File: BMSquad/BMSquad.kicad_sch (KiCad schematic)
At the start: 35 parts, among them J1 USB_C_Receptacle_USB2.0_16P, J2 OUT_1 +, J3 BAT_1 +, J4 OUT_1 -, J5 BAT_1 -, J6 OUT_2 +, J7 OUT_2 -, J8 BAT_2 +, J9 BAT_2 -, U1 TP4056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

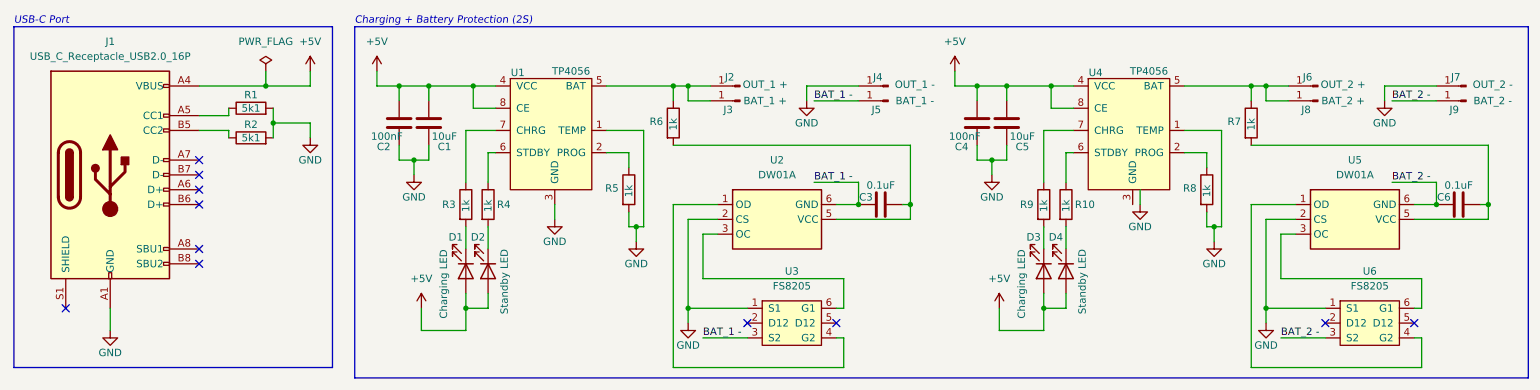
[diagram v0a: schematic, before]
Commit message: added hierarchical sheets
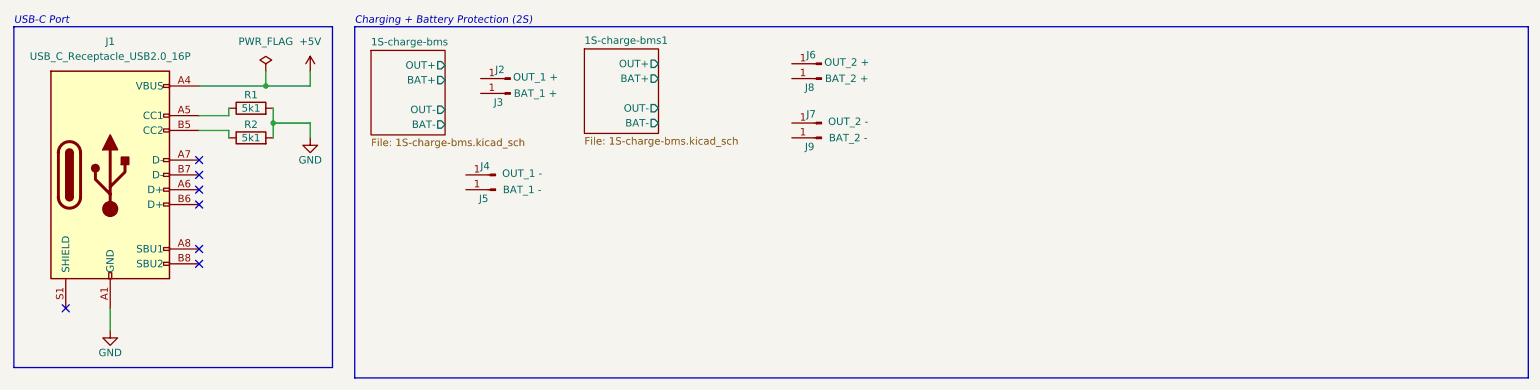
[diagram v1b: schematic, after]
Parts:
- removed C1, C5: 10uF, symbol Device:C
- removed C2, C4: 100nF, symbol Device:C
- removed C3, C6: 0.1uF, symbol Device:C
- removed D1, D3: Charging LED, symbol Device:LED
- removed D2, D4: Standby LED, symbol Device:LED
- removed R10, R3, R4, R5, R6, R7, R8, R9: 1k, symbol Device:R
- removed U1, U4: TP4056, Package_SO:SOP-8-1EP_4.57x4.57mm_P1.27mm_EP4.57x4.45mm, symbol PCM_marbastlib-various:TP4056
- removed U2, U5: DW01A, Package_TO_SOT_SMD:SOT-23-6, symbol Battery_Management:DW01A
- removed U3, U6: FS8205, Package_TO_SOT_SMD:SOT-23-6, symbol PCM_marbastlib-various:FS8205
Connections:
- net GND: no longer J4.1 (Pin_1), J7.1 (Pin_1)
- net at J6.1 (Pin_1): no longer J8.1 (Pin_1)
- net at J2.1 (Pin_1): no longer J3.1 (Pin_1)
- net BAT_1 -: no longer names the net of J5.1 (Pin_1)
- net BAT_2 -: no longer names the net of J9.1 (Pin_1)
- no-connect marks 11 -> 7
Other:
- added sheet 1S-charge-bms (1S-charge-bms.kicad_sch)
- added sheet 1S-charge-bms1 (1S-charge-bms.kicad_sch)
- moved on the sheet: J2, J3, J4, J5, J6, J7, J8, J9
